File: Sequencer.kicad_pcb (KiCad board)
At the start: 2 copper layers, 46.8 x 34.8 mm, 53 parts, among them J1 Screw_Terminal_01x12, J2 Serial_Mode, J3 USB_C_Receptacle_USB2.0_16P, J4 Extra, U1 ATtiny1616-S, U2 TLP3123, U3 TLP3123, U4 TLP3123, U5 TLP3123, U6 MC78L05_SOT89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

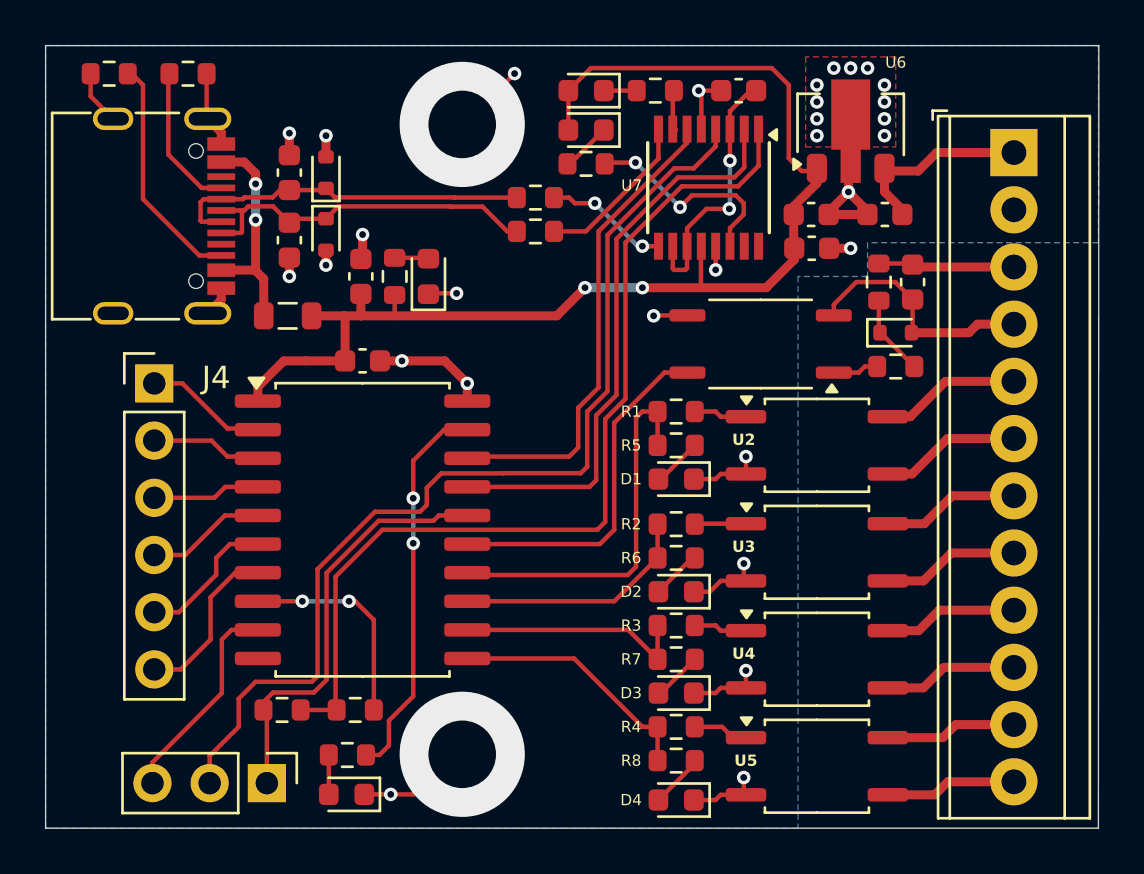
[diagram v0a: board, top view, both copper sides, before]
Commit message: Finalized design for release to JCLPCB Add terminal block library Added some data sheets for terminal block, USB-C connector, etc
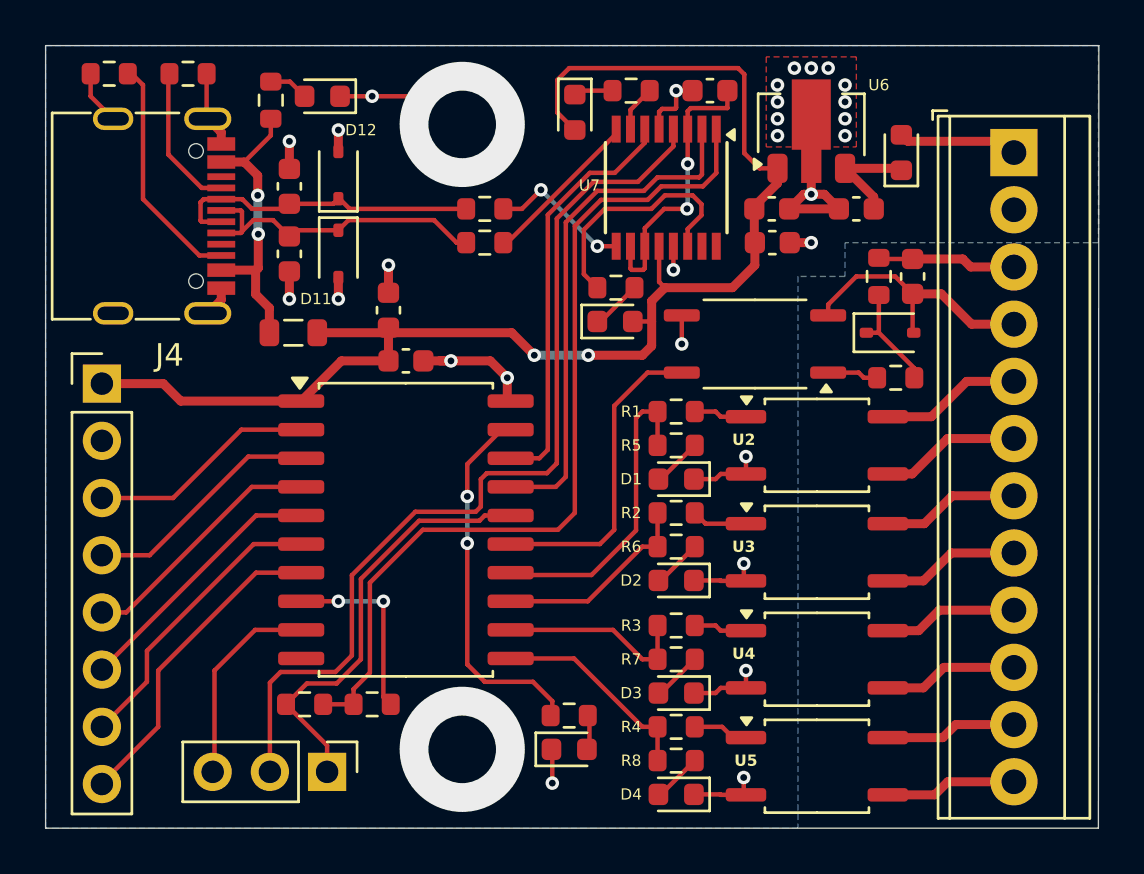
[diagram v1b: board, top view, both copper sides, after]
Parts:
- added D10: D_Schottky, Diode_SMD:D_0603_1608Metric, F.Cu at (170.5, 54.0)
- C2: value 10 -> 10u
- C3, C6, C7, C8, C9: value .1 -> .1u
- C4: value .33 -> .33u
- D11, D12, D5: value DZ2S036X0L -> MM3Z3V6; footprint Diode_SMD:D_SOD-523 -> Diode_SMD:D_SOD-323
- J4: value Extra -> Conn_01x08_Pin; footprint Connector_PinHeader_2.54mm:PinHeader_1x06_P2.54mm_Vertical -> Connector_PinHeader_2.54mm:PinHeader_1x08_P2.54mm_Vertical
- U2, U3, U4, U5: value TLP3123 -> GAQY212G2S
- moved D9 10.1 mm to (155.8, 80.5), turned to 0 degrees
- moved R17 10.0 mm to (155.8, 79.0), turned to 0 degrees
- moved R10 9.56 mm to (142.5, 51.7)
- moved D6 9.28 mm to (144.8, 51.5), turned to 180 degrees
- moved D7 8.60 mm to (157.8, 61.5), turned to 0 degrees
- moved R15 5.66 mm to (157.8, 60.0), turned to 0 degrees
- moved J2 2.72 mm to (145.0, 81.5)
- moved J4 2.33 mm to (135.0, 64.3)
- moved R13 2.30 mm to (152.0, 56.5)
- moved R14 2.30 mm to (152.0, 58.0)
- moved C8 1.94 mm to (147.7, 61.0)
- moved C9 1.93 mm to (148.5, 63.2)
- moved U1 1.93 mm to (148.5, 70.8)
- moved U7 1.88 mm to (160.1, 55.6)
- moved C2 1.77 mm to (164.8, 58.0)
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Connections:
- net Net-(U1-PA3) renamed /LED
- C4 pad 1: /12V -> Net-(D10-K)
- J4 pad 1: Net-(J4-Pin_1) -> /5V
- J4 pad 2: Net-(J4-Pin_2) -> GND
- R10 pad 2: /5V -> Net-(FB1-Pad1)
- U1 pad 2: Net-(J4-Pin_1) -> Net-(J4-Pin_3)
- U1 pad 3: Net-(J4-Pin_2) -> Net-(J4-Pin_4)
- U1 pad 4: Net-(J4-Pin_3) -> Net-(J4-Pin_5)
- U1 pad 5: Net-(J4-Pin_4) -> Net-(J4-Pin_6)
- U1 pad 6: Net-(J4-Pin_5) -> Net-(J4-Pin_7)
- U1 pad 7: Net-(J4-Pin_6) -> Net-(J4-Pin_8)
- U6 pad 3: /12V -> Net-(D10-K)
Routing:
- net Net-(J4-Pin_8): track 0.00 -> 14.2 mm
- net Net-(J4-Pin_7): track 0.00 -> 13.0 mm
- net /5V: track 54.0 -> 61.6 mm
- net Net-(J4-Pin_1): track 5.45 -> 0.00 mm
- net Net-(J4-Pin_4): track 5.33 -> 10.7 mm
- net Net-(J4-Pin_3): track 4.80 -> 10.1 mm
- net Net-(J4-Pin_2): track 4.93 -> 0.00 mm
- net Net-(J4-Pin_5): track 6.29 -> 11.2 mm
- net Net-(D10-K): track 0.00 -> 4.86 mm
- net Net-(J4-Pin_6): track 7.48 -> 11.7 mm
- net /RXD_U: track 45.1 -> 41.7 mm
- net Net-(FB1-Pad1): track 9.75 -> 13.1 mm
- net /12V: track 8.45 -> 5.33 mm
- net /TXD_U: track 42.2 -> 39.4 mm
- net /SEQ1: track 16.9 -> 14.0 mm
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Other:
- board text added: "12V G KEY S4 S3 S2 S1"
- board text added: "5V G PA4 PA5 PA6 PA7 PB5 PB4"
- board text added: "PDI / SER"
- board text added: "Tiny Sequencer (c) wa1hco, 2024 Creative Commons CC-BY-SA v4.0"

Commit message: Added USB-C connector footprints Changed ATTiny from SOIC-20 to 3x3 mm QFP
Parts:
- removed U1: ATtiny1616-S, Package_SO:SOIC-20W_7.5x12.8mm_P1.27mm
- added U9: ATtiny1616-M, Package_DFN_QFN:VQFN-20-1EP_3x3mm_P0.4mm_EP1.7x1.7mm, F.Cu at (151.7, 72.0)
- J2: value Serial_Mode -> Header 1x3
- J3: value USB_C_Receptacle_USB2.0_16P -> USB-C 2.0 16P
- R20: value 1k -> 1K
- moved R17 13.3 mm to (153.2, 66.0), turned to 180 degrees
- moved D9 12.3 mm to (154.0, 68.3), turned to -90 degrees
- moved R11 12.3 mm to (156.0, 76.0)
- moved C9 6.05 mm to (151.5, 68.5)
- moved R12 5.59 mm to (152.0, 76.0), turned to 180 degrees
- moved R15 3.01 mm to (158.0, 63.0)
- moved C8 2.00 mm to (147.7, 59.0)
- moved D7 0.21 mm to (158.0, 61.5), turned to 180 degrees
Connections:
- D9 pad 1: GND -> Net-(D9-K)
- D9 pad 2: Net-(D9-A) -> /LED
- J4 pad 3: Net-(J4-Pin_3) -> /X1
- J4 pad 4: Net-(J4-Pin_4) -> /X2
- J4 pad 5: Net-(J4-Pin_5) -> /X3
- J4 pad 6: Net-(J4-Pin_6) -> /X4
- J4 pad 7: Net-(J4-Pin_7) -> /X5
- J4 pad 8: Net-(J4-Pin_8) -> /X6
- R17 pad 1: /LED -> Net-(D9-K)
- R17 pad 2: Net-(D9-A) -> GND
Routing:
- net /X6: track 0.00 -> 20.5 mm
- net /X5: track 0.00 -> 19.0 mm
- net /X4: track 0.00 -> 17.3 mm
- net /X1: track 0.00 -> 16.4 mm
- net /X3: track 0.00 -> 16.4 mm
- net /X2: track 0.00 -> 15.5 mm
- net Net-(J4-Pin_8): track 14.2 -> 0.00 mm
- net /LED: track 16.5 -> 2.84 mm, vias 2 -> 0
- net Net-(J4-Pin_7): track 13.0 -> 0.00 mm
- net Net-(J4-Pin_6): track 11.7 -> 0.00 mm
- net Net-(J4-Pin_5): track 11.2 -> 0.00 mm
- net Net-(J4-Pin_4): track 10.7 -> 0.00 mm
- net Net-(J4-Pin_3): track 10.1 -> 0.00 mm
- net /TXD_M: track 9.13 -> 16.7 mm, vias 0 -> 2
- net /5V: track 61.6 -> 67.3 mm
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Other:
- board text removed: "Tiny Sequencer (c) wa1hco, 2024 Creative Commons CC-BY-SA v4.0"
